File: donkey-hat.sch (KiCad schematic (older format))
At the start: 59 parts, among them J1 6-18V, J14 NEOPIXEL, J15 MPU-9250, J16 4, J17 5, J18 6, J19 7, J2 Raspberry_Pi_2_3, J24 3mm_Mount, J25 3mm_Mount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

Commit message: Checking libs, project paths.
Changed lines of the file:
@@
 EESchema Schematic File Version 4
 LIBS:donkey-hat-cache
-EELAYER 26 0
+EELAYER 30 0
 EELAYER END
 $Descr A4 11693 8268
@@
 F 1 "MPM3632C" H 4475 6237 50  0000 C CNN
 F 2 "libs:mpm3632c" H 4500 5450 50  0001 C CNN
-F 3 "https://media.monolithicpower.com/document/m/p/mpm3632c_r1.0.pdf" H 4500 5450 50  0001 C CNN
+F 3 "https://www.monolithicpower.com/en/documentview/productdocument/index/version/2/document_type/Datasheet/lang/en/sku/MPM3632CGQV/document_id/4349/" H 4500 5450 50  0001 C CNN
 F 4 "https://www.digikey.com/product-detail/en/monolithic-power-systems-inc/MPM3632CGQV-Z/1589-1955-1-ND/9637668" H 4500 5450 50  0001 C CNN "Link"
 F 5 "20-QFN" H 0   0   50  0001 C CNN "Package"
@@
 Wire Wire Line
 	4650 4750 4550 4750
-Connection ~ 4450 4750
-Wire Wire Line
-	4450 4750 4350 4750
 Connection ~ 4550 4750
 Wire Wire Line
 	4550 4750 4450 4750
-Wire Wire Line
-	5150 5450 5200 5450
-Wire Wire Line
-	5200 5450 5200 5350
-Wire Wire Line
-	5200 5350 5150 5350
 $Comp
 L Device:R R14
@@
 Wire Wire Line
 	5600 5550 5600 5350
-Wire Wire Line
-	5600 5350 5200 5350
-Connection ~ 5200 5350
 $Comp
 L Device:C C4
@@
 $EndComp
 Wire Wire Line
-	5150 5650 5750 5650
-Wire Wire Line
 	5750 5700 5750 5650
-Connection ~ 5750 5650
 $Comp
 L Device:C C2
@@
 Wire Wire Line
 	3000 5250 3000 5550
+Connection ~ 5750 5650
+Wire Wire Line
+	5150 5650 5750 5650
+Wire Wire Line
+	5150 5350 5600 5350
 $EndSCHEMATC

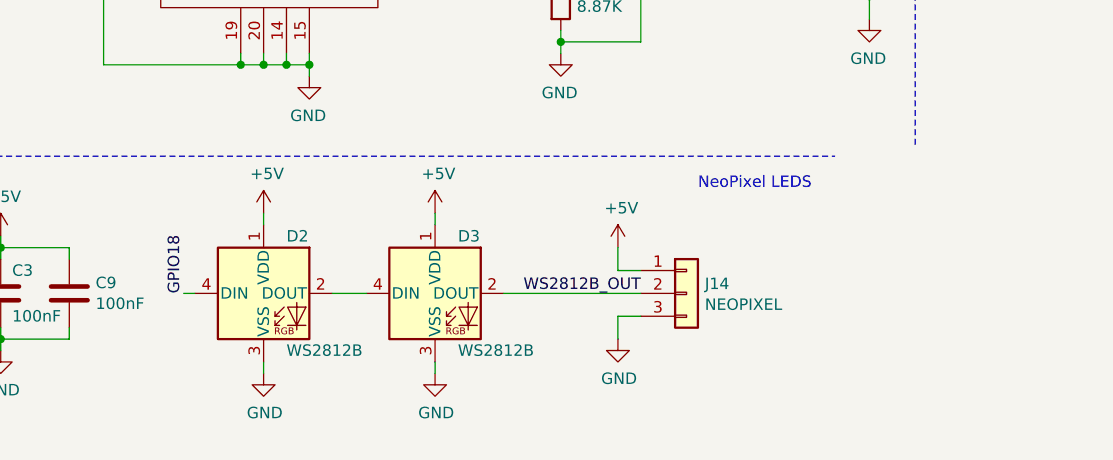
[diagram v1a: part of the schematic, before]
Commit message: Remove ws2812. Keep header.
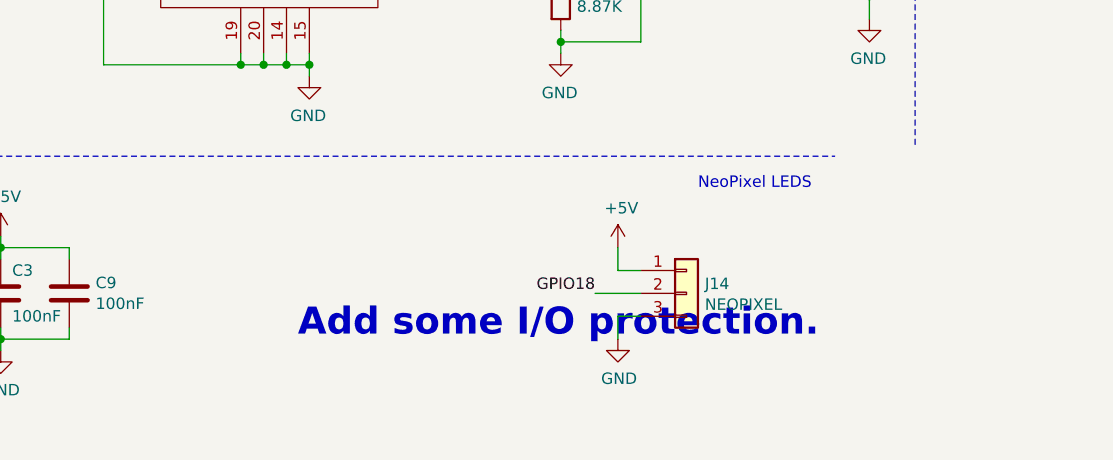
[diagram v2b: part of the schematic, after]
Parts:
- removed D2, D3: WS2812B, LED_SMD:LED_WS2812B_PLCC4_5.0x5.0mm_P3.2mm, symbol LED:WS2812B
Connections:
- net WS2812B_OUT is gone; now on net GPIO18: J14.2 (Pin_2)
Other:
- note added: "Add some I/O protection."
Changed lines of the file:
@@
 	7100 5850 7100 5750
-$Comp
-L LED:WS2812B D2
-U 1 1 5C31B762
-P 4450 7150
-F 0 "D2" H 4550 7400 50  0000 L CNN
-F 1 "WS2812B" H 4550 6900 50  0000 L CNN
-F 2 "LED_SMD:LED_WS2812B_PLCC4_5.0x5.0mm_P3.2mm" H 4500 6850 50  0001 L TNN
-F 3 "https://cdn-shop.adafruit.com/datasheets/WS2812B.pdf" H 4550 6775 50  0001 L TNN
-F 4 "SMD" H 0   0   50  0001 C CNN "Package"
-F 5 "Worldsemi" H 0   0   50  0001 C CNN "Manufacturer"
-F 6 "WS2812B" H 0   0   50  0001 C CNN "Mfg Part #"
-	1    4450 7150
-	1    0    0    -1
-$EndComp
-Wire Wire Line
-	4100 7150 4150 7150
-$Comp
-L power:GND #PWR0128
-U 1 1 5C33445D
-P 4450 7500
-F 0 "#PWR0128" H 4450 7250 50  0001 C CNN
-F 1 "GND" H 4455 7327 50  0000 C CNN
-F 2 "" H 4450 7500 50  0001 C CNN
-F 3 "" H 4450 7500 50  0001 C CNN
-	1    4450 7500
-	1    0    0    -1
-$EndComp
-$Comp
-L power:+5V #PWR0129
-U 1 1 5C3345B1
-P 4450 6800
-F 0 "#PWR0129" H 4450 6650 50  0001 C CNN
-F 1 "+5V" H 4465 6973 50  0000 C CNN
-F 2 "" H 4450 6800 50  0001 C CNN
-F 3 "" H 4450 6800 50  0001 C CNN
-	1    4450 6800
-	1    0    0    -1
-$EndComp
-Text Label 6100 7150 2    50   ~ 0
-WS2812B_OUT
-$Comp
-L LED:WS2812B D3
-U 1 1 5C334A57
-P 5200 7150
-F 0 "D3" H 5300 7400 50  0000 L CNN
-F 1 "WS2812B" H 5300 6900 50  0000 L CNN
-F 2 "LED_SMD:LED_WS2812B_PLCC4_5.0x5.0mm_P3.2mm" H 5250 6850 50  0001 L TNN
-F 3 "https://cdn-shop.adafruit.com/datasheets/WS2812B.pdf" H 5300 6775 50  0001 L TNN
-F 4 "SMD" H 0   0   50  0001 C CNN "Package"
-F 5 "Worldsemi" H 0   0   50  0001 C CNN "Manufacturer"
-F 6 "WS2812B" H 0   0   50  0001 C CNN "Mfg Part #"
-	1    5200 7150
-	1    0    0    -1
-$EndComp
-Wire Wire Line
-	4750 7150 4900 7150
-Wire Wire Line
-	4450 6850 4450 6800
-Wire Wire Line
-	4450 7450 4450 7500
-$Comp
-L power:+5V #PWR0130
-U 1 1 5C37EF3C
-P 5200 6800
-F 0 "#PWR0130" H 5200 6650 50  0001 C CNN
-F 1 "+5V" H 5215 6973 50  0000 C CNN
-F 2 "" H 5200 6800 50  0001 C CNN
-F 3 "" H 5200 6800 50  0001 C CNN
-	1    5200 6800
-	1    0    0    -1
-$EndComp
-Wire Wire Line
-	5200 6850 5200 6800
-$Comp
-L power:GND #PWR0131
-U 1 1 5C397ECA
-P 5200 7500
-F 0 "#PWR0131" H 5200 7250 50  0001 C CNN
-F 1 "GND" H 5205 7327 50  0000 C CNN
-F 2 "" H 5200 7500 50  0001 C CNN
-F 3 "" H 5200 7500 50  0001 C CNN
-	1    5200 7500
-	1    0    0    -1
-$EndComp
-Wire Wire Line
-	5200 7450 5200 7500
-Wire Wire Line
-	6100 7150 5500 7150
 $Comp
 L Device:C C3
@@
 Text Notes 800  750  0    50   ~ 0
 Raspberry Pi
-Text Label 4100 7150 1    50   ~ 0
+Text Label 5900 7150 2    50   ~ 0
 GPIO18
 Wire Notes Line
@@
 Wire Wire Line
 	5150 5350 5600 5350
+Wire Wire Line
+	6100 7150 5900 7150
+Text Notes 4600 7350 0    118  ~ 24
+Add some I/O protection.
 $EndSCHEMATC
